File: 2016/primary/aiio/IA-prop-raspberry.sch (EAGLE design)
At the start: 94 parts, among them U1 ARDUINO_R3_SHIELD

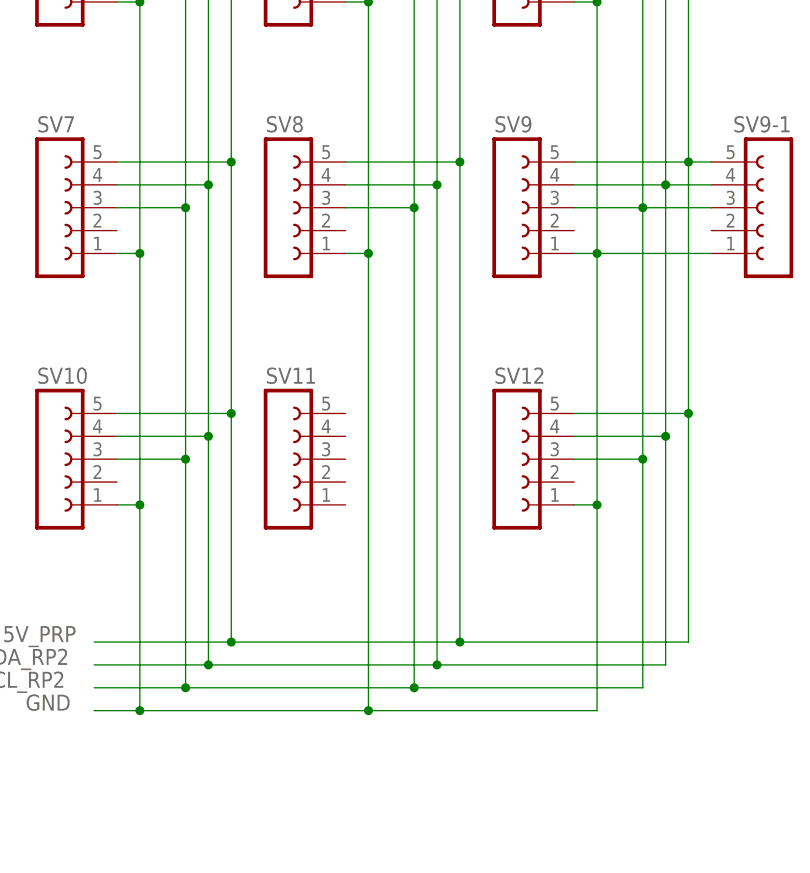
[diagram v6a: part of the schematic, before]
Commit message: [AIIO_board] Make route for sonar I2C
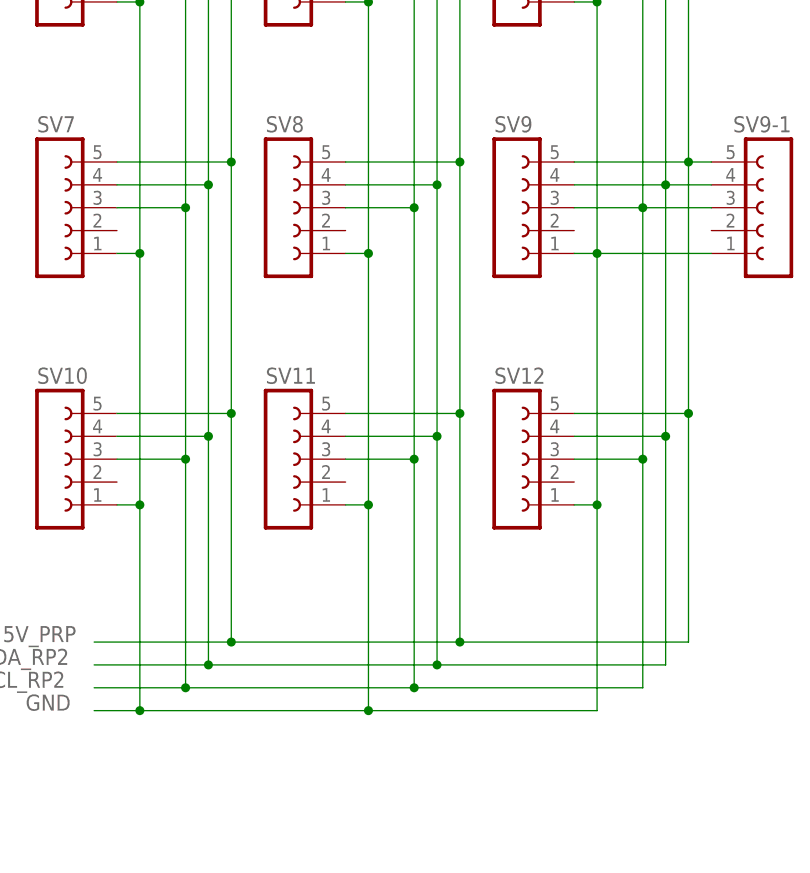
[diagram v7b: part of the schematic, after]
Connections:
- net 5V_PRP: now also SV11.5
- net GND: now also SV11.1
- net SCL_RP2: now also SV11.3
- net SDA_RP2: now also SV11.4
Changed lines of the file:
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@@
 <wire x1="325.12" y1="66.04" x2="325.12" y2="40.64" width="0.1524" layer="91"/>
 <wire x1="325.12" y1="40.64" x2="325.12" y2="12.7" width="0.1524" layer="91"/>
-<wire x1="325.12" y1="12.7" x2="325.12" y2="-40.64" width="0.1524" layer="91"/>
+<wire x1="325.12" y1="12.7" x2="325.12" y2="-15.24" width="0.1524" layer="91"/>
+<wire x1="325.12" y1="-15.24" x2="325.12" y2="-40.64" width="0.1524" layer="91"/>
 <wire x1="299.72" y1="-40.64" x2="325.12" y2="-40.64" width="0.1524" layer="91"/>
 <pinref part="SV3" gate="G$1" pin="5"/>
@@
 <pinref part="SV9-1" gate="G$1" pin="5"/>
 <wire x1="353.06" y1="12.7" x2="350.52" y2="12.7" width="0.1524" layer="91"/>
+<pinref part="SV11" gate="G$1" pin="5"/>
+<wire x1="312.42" y1="-15.24" x2="325.12" y2="-15.24" width="0.1524" layer="91"/>
+<junction x="325.12" y="-15.24"/>
 </segment>
 </net>
@@
 <wire x1="314.96" y1="55.88" x2="314.96" y2="30.48" width="0.1524" layer="91"/>
 <wire x1="314.96" y1="30.48" x2="314.96" y2="2.54" width="0.1524" layer="91"/>
-<wire x1="314.96" y1="2.54" x2="314.96" y2="-48.26" width="0.1524" layer="91"/>
+<wire x1="314.96" y1="2.54" x2="314.96" y2="-25.4" width="0.1524" layer="91"/>
+<wire x1="314.96" y1="-25.4" x2="314.96" y2="-48.26" width="0.1524" layer="91"/>
 <wire x1="340.36" y1="-48.26" x2="314.96" y2="-48.26" width="0.1524" layer="91"/>
 <pinref part="SV1" gate="G$1" pin="1"/>
@@
 <pinref part="SV9-1" gate="G$1" pin="1"/>
 <wire x1="353.06" y1="2.54" x2="340.36" y2="2.54" width="0.1524" layer="91"/>
+<pinref part="SV11" gate="G$1" pin="1"/>
+<wire x1="312.42" y1="-25.4" x2="314.96" y2="-25.4" width="0.1524" layer="91"/>
+<junction x="314.96" y="-25.4"/>
 </segment>
 </net>
@@
 <wire x1="320.04" y1="60.96" x2="320.04" y2="35.56" width="0.1524" layer="91"/>
 <wire x1="320.04" y1="35.56" x2="320.04" y2="7.62" width="0.1524" layer="91"/>
-<wire x1="320.04" y1="7.62" x2="320.04" y2="-45.72" width="0.1524" layer="91"/>
+<wire x1="320.04" y1="7.62" x2="320.04" y2="-20.32" width="0.1524" layer="91"/>
+<wire x1="320.04" y1="-20.32" x2="320.04" y2="-45.72" width="0.1524" layer="91"/>
 <wire x1="345.44" y1="-45.72" x2="320.04" y2="-45.72" width="0.1524" layer="91"/>
 <pinref part="SV1" gate="G$1" pin="3"/>
@@
 <pinref part="SV9-1" gate="G$1" pin="3"/>
 <wire x1="353.06" y1="7.62" x2="345.44" y2="7.62" width="0.1524" layer="91"/>
+<pinref part="SV11" gate="G$1" pin="3"/>
+<wire x1="312.42" y1="-20.32" x2="320.04" y2="-20.32" width="0.1524" layer="91"/>
+<junction x="320.04" y="-20.32"/>
 </segment>
 <segment>
@@
 <wire x1="322.58" y1="63.5" x2="322.58" y2="38.1" width="0.1524" layer="91"/>
 <wire x1="322.58" y1="38.1" x2="322.58" y2="10.16" width="0.1524" layer="91"/>
-<wire x1="322.58" y1="10.16" x2="322.58" y2="-43.18" width="0.1524" layer="91"/>
+<wire x1="322.58" y1="10.16" x2="322.58" y2="-17.78" width="0.1524" layer="91"/>
+<wire x1="322.58" y1="-17.78" x2="322.58" y2="-43.18" width="0.1524" layer="91"/>
 <wire x1="347.98" y1="-43.18" x2="322.58" y2="-43.18" width="0.1524" layer="91"/>
 <pinref part="SV1" gate="G$1" pin="4"/>
@@
 <pinref part="SV9-1" gate="G$1" pin="4"/>
 <wire x1="353.06" y1="10.16" x2="347.98" y2="10.16" width="0.1524" layer="91"/>
-</segment>
-<segment>
+<pinref part="SV11" gate="G$1" pin="4"/>
+<wire x1="312.42" y1="-17.78" x2="322.58" y2="-17.78" width="0.1524" layer="91"/>
+<junction x="322.58" y="-17.78"/>
+</segment>
+<segment>

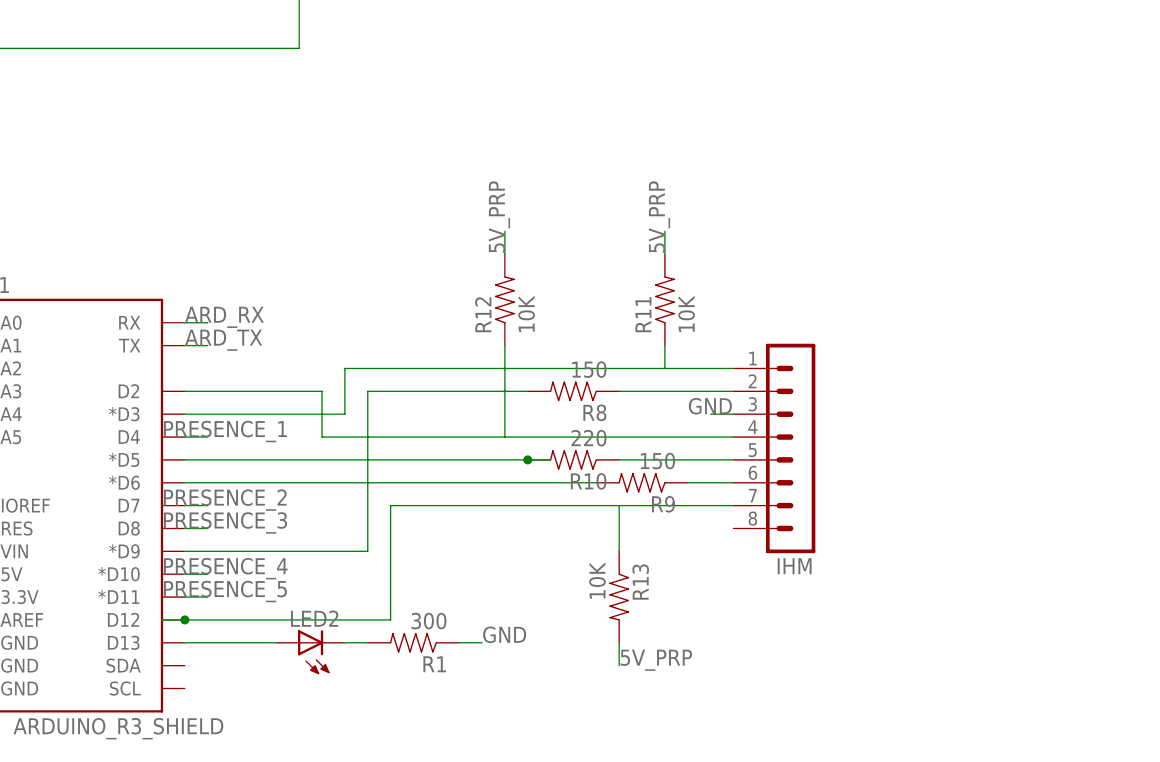
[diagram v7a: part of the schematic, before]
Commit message: [AIIO_board] Update pin Ardu
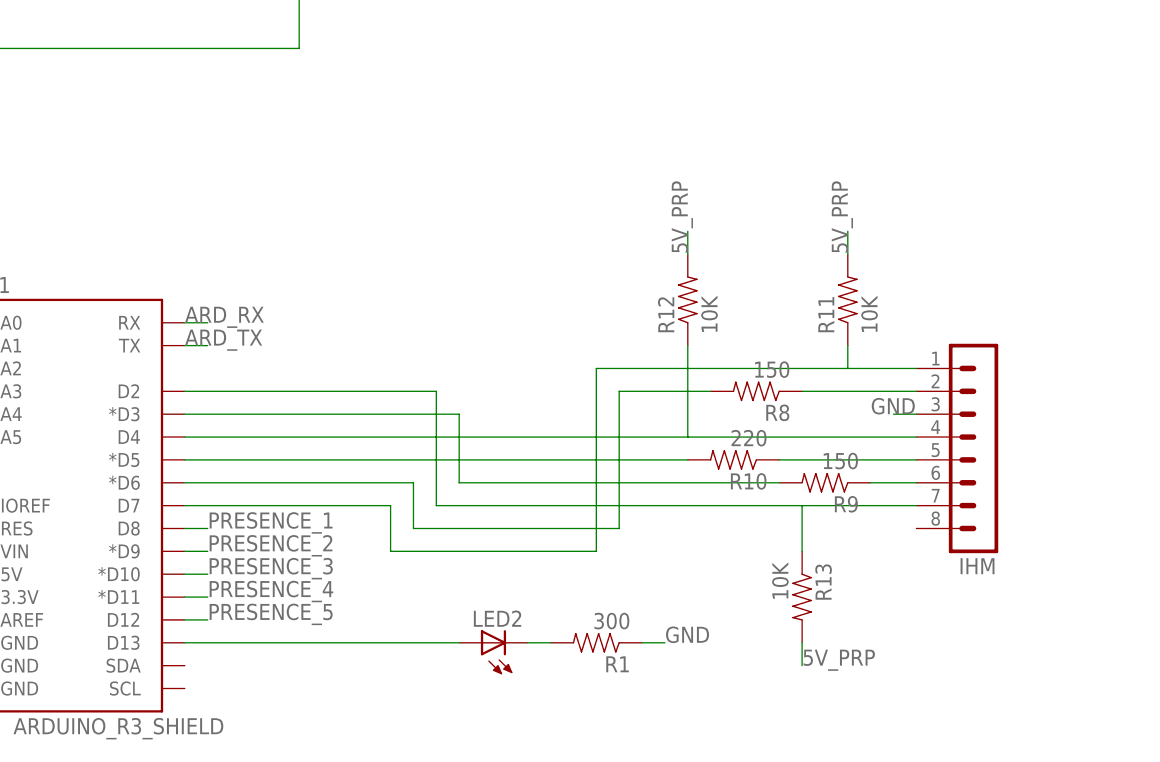
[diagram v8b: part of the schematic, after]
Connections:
- removed net N$40: R9.2, U1.*D6
- new net N$17: R9.2, U1.*D3
- net N$45: now also U1.*D6; no longer U1.*D9
- net N$46: now also U1.D7; no longer U1.*D3
- net N$47: now also U1.D4; no longer U1.D2
- net N$49: now also U1.D2; no longer U1.D12
- net PRESENCE_1: now also U1.D8; no longer U1.D4
- net PRESENCE_2: now also U1.*D9; no longer U1.D7
- net PRESENCE_3: now also U1.*D10; no longer U1.D8
- net PRESENCE_4: now also U1.*D11; no longer U1.*D10
- net PRESENCE_5: now also U1.D12; no longer U1.*D11
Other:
- moved on the sheet: IHM, LED2, R1, R10, R11, R12, R13, R8, R9
